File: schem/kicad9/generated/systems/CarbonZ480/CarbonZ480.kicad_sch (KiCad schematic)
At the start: 0 parts

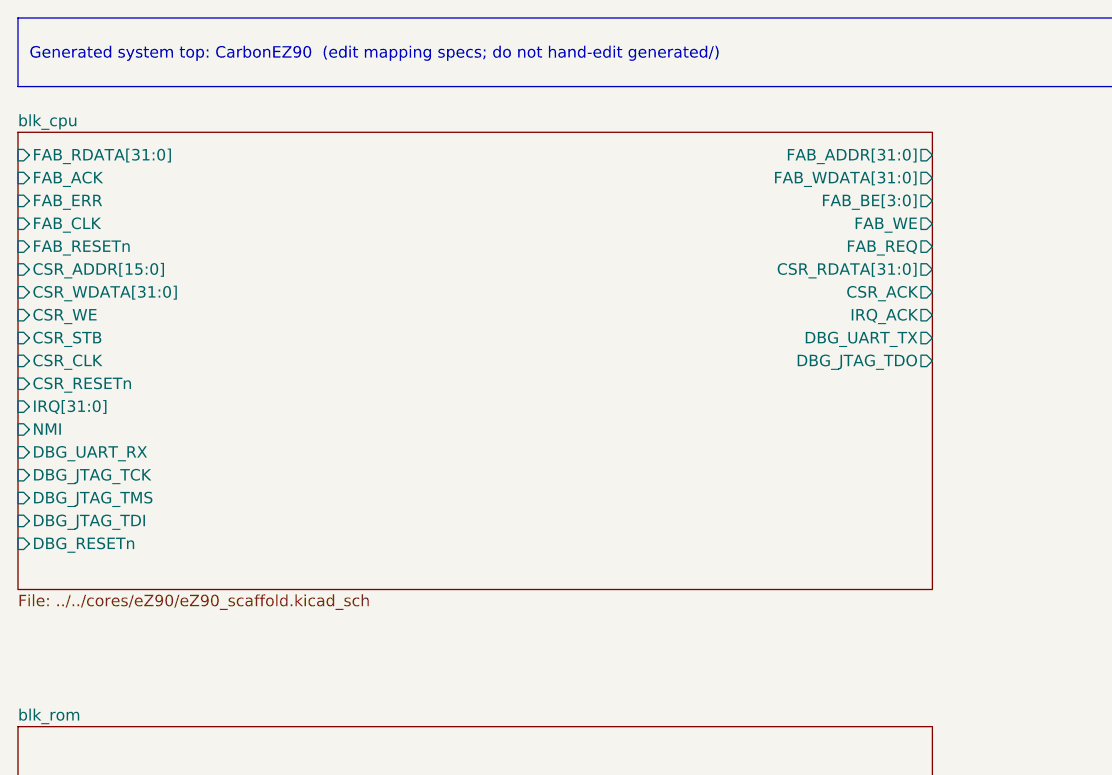
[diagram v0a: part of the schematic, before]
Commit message: systems: rename CarbonEZ90 to CarbonZ480 and refresh maps
Detailed description:
- What changed: renamed the CarbonEZ90 system to CarbonZ480, updated system tops for Z480 tier IDs and boot signatures, refreshed memory map docs and carbon_memmap_pkg, and updated KiCad kicadgen specs plus regenerated Z480/CarbonZ480 schematics.
- Why it changed: keep system naming, maps, and schematics consistent with the new Z480 tier model.
- Files/paths affected: hdl/systems/CarbonZ480/*, hdl/systems/CarbonEZ90/* (removed), hdl/systems/CarbonZ80/*, hdl/systems/CarbonZ90/*, hdl/systems/CarbonX86/*, hdl/systems/CarbonX96/*, hdl/systems/common/rtl/carbon_memmap_pkg.sv, schem/kicad9/spec/kicadgen_*.yaml, schem/kicad9/generated/cores/Z480, schem/kicad9/generated/systems/CarbonZ480.
- Any compatibility notes: reset still enters P0; Z480 presents as P7; memory map ranges stay stable aside from naming.
- What remains TODO: update sim harnesses and documentation references to the new names.
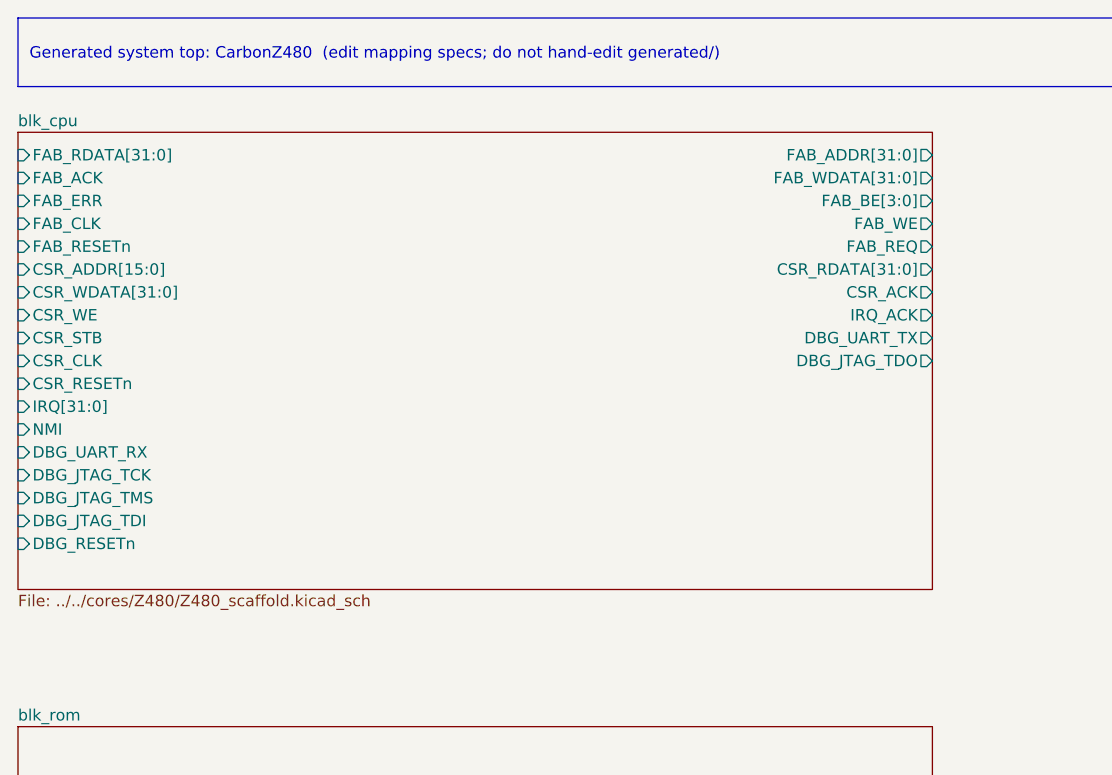
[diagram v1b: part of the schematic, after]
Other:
- sheet blk_cpu: file ../../cores/eZ90/eZ90_scaffold.kicad_sch -> ../../cores/Z480/Z480_scaffold.kicad_sch
- title: CarbonEZ90 (generated) -> CarbonZ480 (generated)
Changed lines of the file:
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@@
 	(paper "A3")
 	(title_block
-		(title "CarbonEZ90 (generated)")
+		(title "CarbonZ480 (generated)")
 		(company "Project Carbon")
 		(comment 1 "Generated - do not edit in generated/")
@@
 	)
 	(text_box
-		"Generated system top: CarbonEZ90  (edit mapping specs; do not hand-edit generated/)"
+		"Generated system top: CarbonZ480  (edit mapping specs; do not hand-edit generated/)"
 		(exclude_from_sim no)
 		(at
@@
 		(property
 			"Sheetfile"
-			"../../cores/eZ90/eZ90_scaffold.kicad_sch"
+			"../../cores/Z480/Z480_scaffold.kicad_sch"
 			(at
 				12.7
@@
 		(instances
 			(project
-				"system_CarbonEZ90"
+				"system_CarbonZ480"
 				(path
 					"/17675ba5-bcbf-5d72-8a1b-6c49952c9687"
@@
 		(instances
 			(project
-				"system_CarbonEZ90"
+				"system_CarbonZ480"
 				(path
 					"/17675ba5-bcbf-5d72-8a1b-6c49952c9687"
@@
 		(instances
 			(project
-				"system_CarbonEZ90"
+				"system_CarbonZ480"
 				(path
 					"/17675ba5-bcbf-5d72-8a1b-6c49952c9687"
@@
 		(instances
 			(project
-				"system_CarbonEZ90"
+				"system_CarbonZ480"
 				(path
 					"/17675ba5-bcbf-5d72-8a1b-6c49952c9687"
@@
 		(instances
 			(project
-				"system_CarbonEZ90"
+				"system_CarbonZ480"
 				(path
 					"/17675ba5-bcbf-5d72-8a1b-6c49952c9687"
@@
 		(instances
 			(project
-				"system_CarbonEZ90"
+				"system_CarbonZ480"
 				(path
 					"/17675ba5-bcbf-5d72-8a1b-6c49952c9687"
@@
 		(instances
 			(project
-				"system_CarbonEZ90"
+				"system_CarbonZ480"
 				(path
 					"/17675ba5-bcbf-5d72-8a1b-6c49952c9687"
@@
 		(instances
 			(project
-				"system_CarbonEZ90"
+				"system_CarbonZ480"
 				(path
 					"/17675ba5-bcbf-5d72-8a1b-6c49952c9687"
@@
 		(instances
 			(project
-				"system_CarbonEZ90"
+				"system_CarbonZ480"
 				(path
 					"/17675ba5-bcbf-5d72-8a1b-6c49952c9687"
@@
 		(instances
 			(project
-				"system_CarbonEZ90"
+				"system_CarbonZ480"
 				(path
 					"/17675ba5-bcbf-5d72-8a1b-6c49952c9687"
@@
 		(instances
 			(project
-				"system_CarbonEZ90"
+				"system_CarbonZ480"
 				(path
 					"/17675ba5-bcbf-5d72-8a1b-6c49952c9687"

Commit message: kicad: generate Carbon system hierarchical schematics
Detailed description:
- What changed: generated CarbonZ80/Z90/Z380/Z480 system schematics with CPU/FPU, memory, fabric, and platform blocks
- Why it changed: align system-level schematics with the final Z* lineage and Am95xx personalities
- Files/paths affected: schem/kicad9/generated/systems/CarbonZ80/CarbonZ80.kicad_sch, schem/kicad9/generated/systems/CarbonZ90/CarbonZ90.kicad_sch, schem/kicad9/generated/systems/CarbonZ380/CarbonZ380.kicad_sch, schem/kicad9/generated/systems/CarbonZ480/CarbonZ480.kicad_sch
- How to run it: scripts/gen_kicad.sh (or python tools/kicadgen/src/kicadgen.py)
- What remains TODO: update generator docs and add consistency checks for schematic outputs
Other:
- removed sheet blk_rc2014_adapter
- removed sheet blk_s100_adapter
- added sheet blk_CarbonDMA (../../cores/CarbonDMA/CarbonDMA.kicad_sch)
- added sheet blk_CarbonIO (../../cores/CarbonIO/CarbonIO.kicad_sch)
- added sheet blk_fabric (../../common/blk_fabric.kicad_sch)
- added sheet blk_mmio (../../common/blk_mmio.kicad_sch)
- sheet blk_accel: file ../../cores/Am9513/Am9513.kicad_sch -> ../../cores/Am95xx/Am95xx.kicad_sch
- sheet blk_cpu: file ../../cores/Z480/Z480_scaffold.kicad_sch -> ../../cores/Z480/Z480.kicad_sch
